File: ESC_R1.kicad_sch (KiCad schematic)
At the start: 0 parts

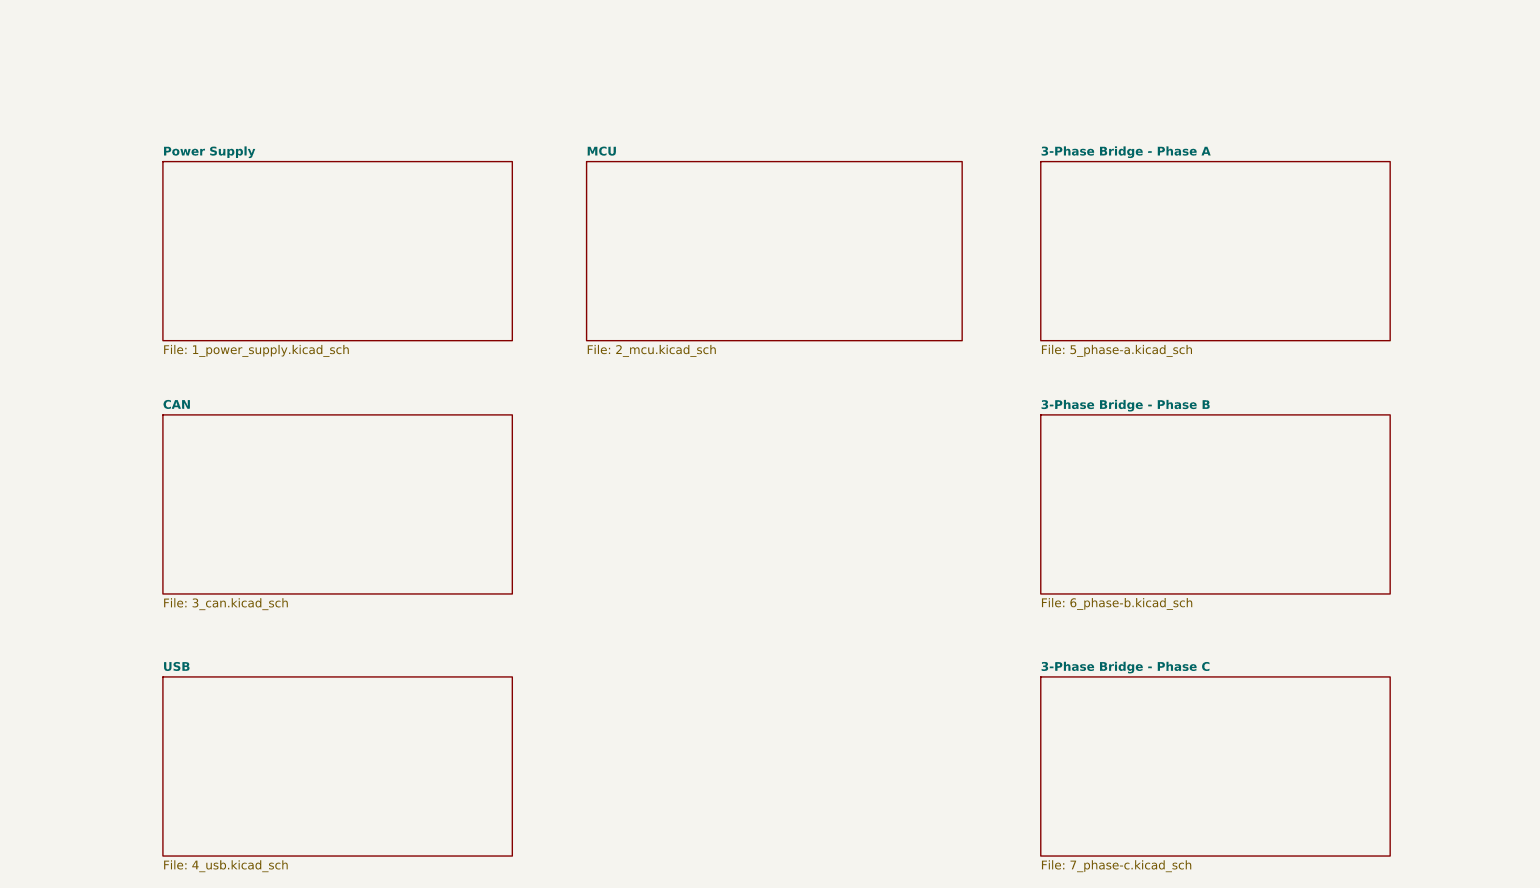
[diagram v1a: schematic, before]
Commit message: feat: major circuit rework, style update and addition of a few extra subcomponents
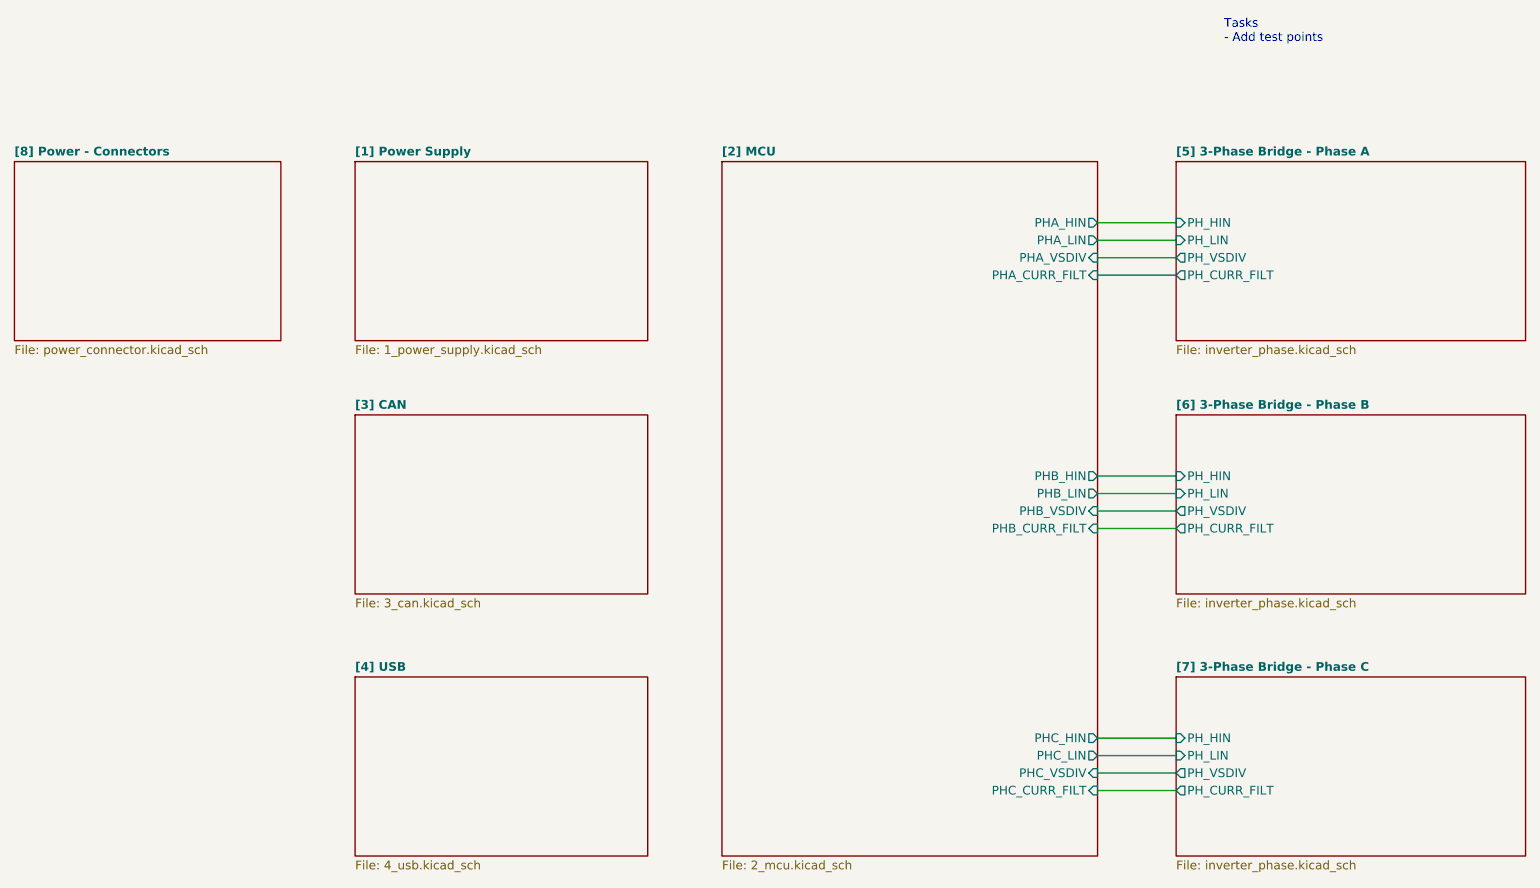
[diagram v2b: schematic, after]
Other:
- sheet 3-Phase Bridge - Phase A renamed [5] 3-Phase Bridge - Phase A
- sheet CAN renamed [3] CAN
- sheet MCU renamed [2] MCU
- sheet Power Supply renamed [1] Power Supply
- sheet USB renamed [4] USB
- removed sheet 3-Phase Bridge - Phase B
- removed sheet 3-Phase Bridge - Phase C
- added sheet [6] 3-Phase Bridge - Phase B (inverter_phase.kicad_sch)
- added sheet [7] 3-Phase Bridge - Phase C (inverter_phase.kicad_sch)
- added sheet [8] Power - Connectors (power_connector.kicad_sch)
- sheet [2] MCU ports: added PHA_CURR_FILT, PHA_HIN, PHA_LIN, PHA_VSDIV, PHB_CURR_FILT, PHB_HIN, PHB_LIN, PHB_VSDIV, PHC_CURR_FILT, PHC_HIN, PHC_LIN, PHC_VSDIV; removed none
- sheet [5] 3-Phase Bridge - Phase A: file 5_phase-a.kicad_sch -> inverter_phase.kicad_sch
- sheet [5] 3-Phase Bridge - Phase A ports: added PH_CURR_FILT, PH_HIN, PH_LIN, PH_VSDIV; removed none
- note added: "Tasks - Add test points"

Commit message: chore: project update
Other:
- note removed: "Tasks - Add test points"
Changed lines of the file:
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@@
     (stroke (width 0) (type default))
-  )
-  (text "Tasks\n- Add test points" (at 208.915 30.48 0)
-    (effects (font (size 1.27 1.27)) (justify left bottom))
   )
   (sheet (at 82.55 122.555) (size 42.545 26.035) (fields_autoplaced)
